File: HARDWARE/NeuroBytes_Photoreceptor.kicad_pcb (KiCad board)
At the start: 2 copper layers, 46.8 x 19.8 mm, 22 parts, among them P1 CONN_01X04, P2 CONN_01X04, P3 CONN_01X07, SW1 SW_PUSH, SW2 SW_PUSH, U1 APDS9007, U2 STM32L011Gx, U3 LD3985M33R

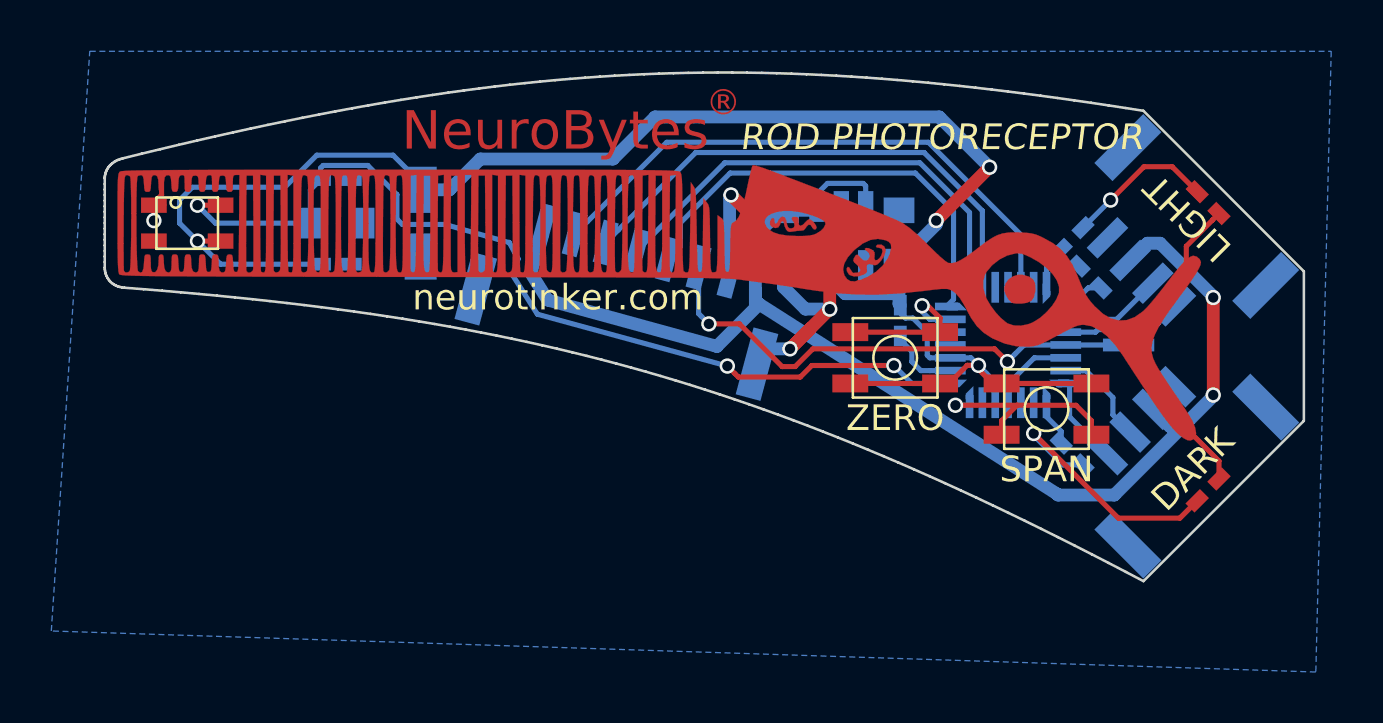
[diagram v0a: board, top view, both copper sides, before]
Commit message: Updated Gerber files. Added BOM. Added component values to schematic. Added fiducials.
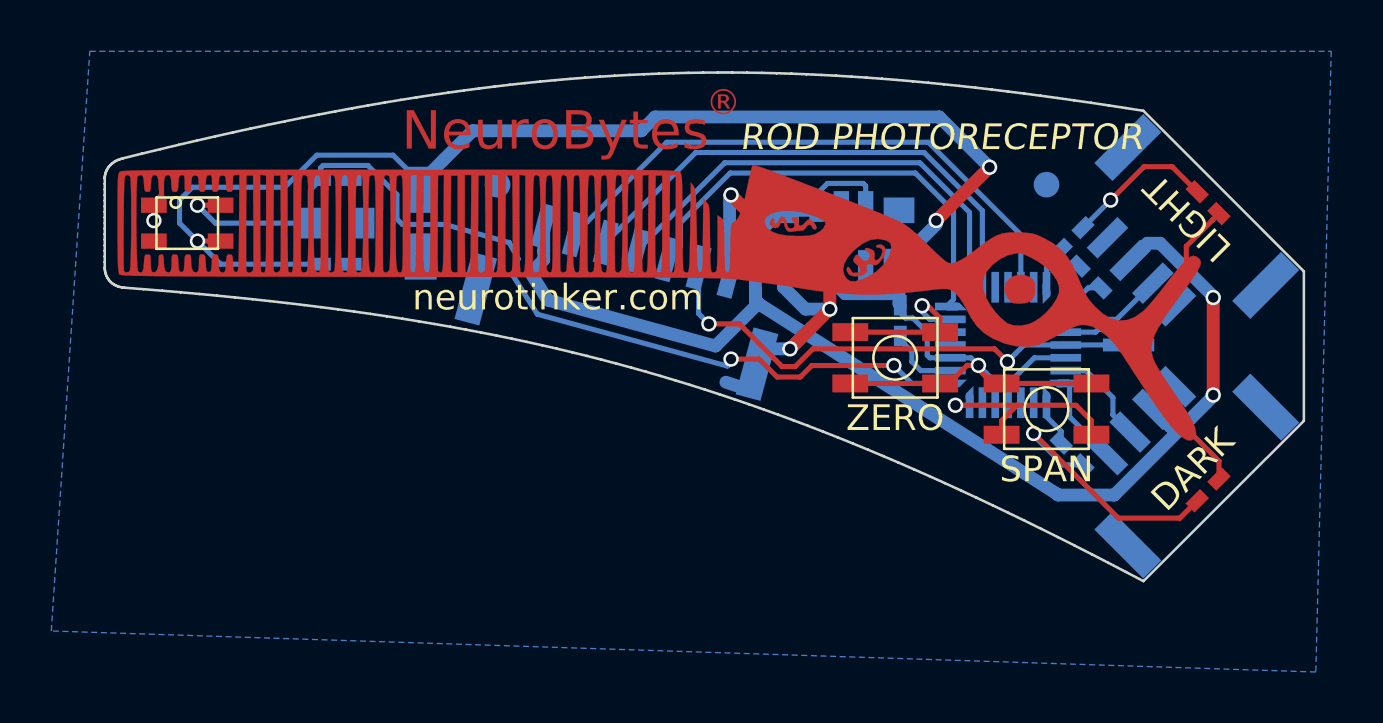
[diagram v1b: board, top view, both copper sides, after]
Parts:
- added REF**: ZF_Fiducial-1mm, KiCad_Footprints:ZF_Fiducial-1mm, B.Cu at (201.5, 94.5)
- added REF**: ZF_Fiducial-1mm, KiCad_Footprints:ZF_Fiducial-1mm, B.Cu at (180.1, 94.5)
- turned U1 to 270 degrees
- turned U2 to 270 degrees
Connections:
- P1 pad : (no net) -> GND
- P2 pad : (no net) -> GND
- P3 pad : (no net) -> GND
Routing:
- net GND: track 49.9 -> 51.9 mm
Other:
- board text added: "COMPONENT POSITION ORIGIN"
- board text added: "NOTES: 1. FOOTPRINTS ORIENTED PER IPC-7351FC LEVEL B (PIN 1 IN LOWER LEFT) 2. COMPONENT ROTATION IN DEGREES COUNTER-CLOCKWISE 3. NOTE COMPONENTS ARE MOUNTED ON BOTH F.CU AND B.CU LAYER 4. PCB IS 1.6mm FR4 RATED FOR ROHS REFLOW, 10Z COPPER, ENIG FINISH 5. MATTE BLACK SOLDER MASK WITH WHITE SILKSCREEN 6. SOLDER PASTE MUST BE ROHS COMPLIANT (LEAD-FREE) 7. NO MARKS (E-TEST, QA, SERIAL NUMBER, ETC) ON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"
- board text added: "ROUTE BOARD OUTLINE EXCEPT FOR TWO ENDS"
- board text added: "V-SCORE PARALLEL ENDS"

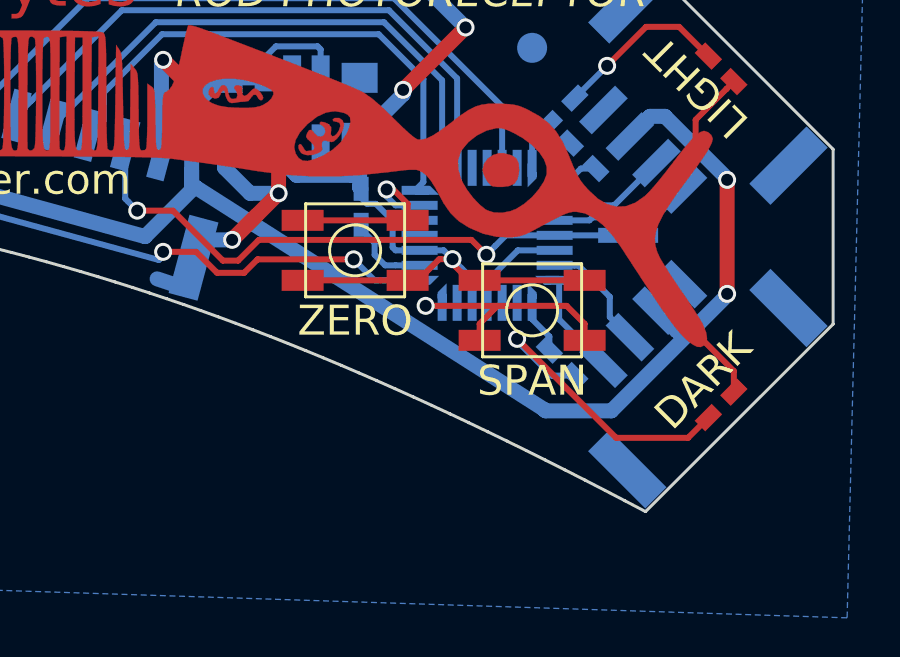
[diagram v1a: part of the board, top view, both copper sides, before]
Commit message: Updated swith footprint.
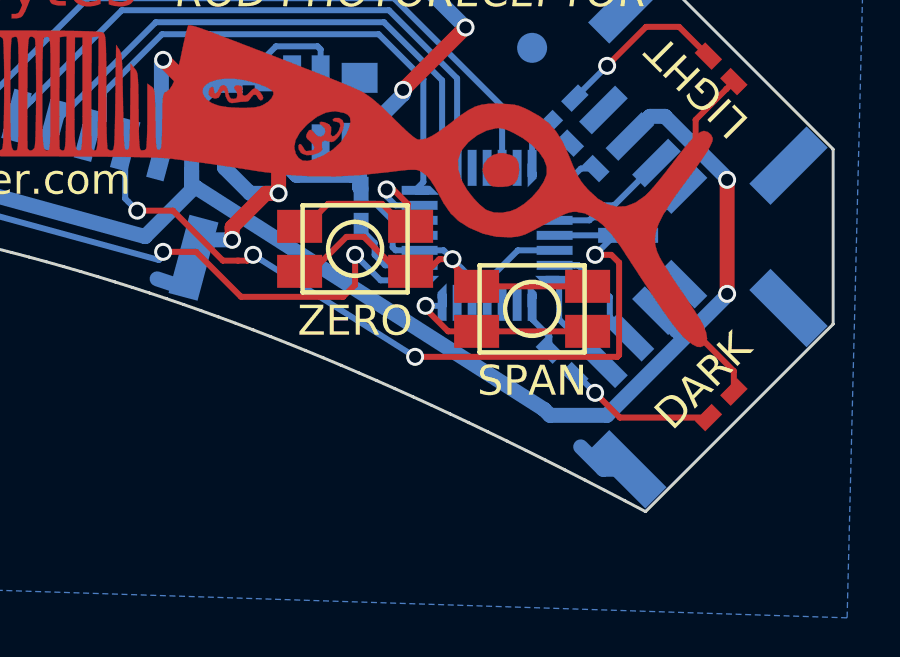
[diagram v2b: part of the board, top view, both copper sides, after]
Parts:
- C1, C2, C6: value C -> 100 nF
- C3, C4, C5: value C -> 1 uF
- C7: value CP -> 10 uF
- R1: value R -> 27k
- R2, R3: value R -> 10
- R4: value R -> JMP
- SW1, SW2: footprint KiCad_Footprints:ZF_SW_LS38 -> KiCad_Footprints:ZF_SW_EVP-AA
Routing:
- net RESET: track 20.0 -> 27.3 mm, vias 2 -> 4
- net Net-(D2-Pad2): track 10.5 -> 5.03 mm
- net SPAN: track 8.49 -> 7.00 mm
- net SENSE: track 37.9 -> 39.2 mm
- net +3V3: track 72.7 -> 74.1 mm
- net GND: track 51.9 -> 52.9 mm
- net ZERO: track 6.40 -> 7.22 mm

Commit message: Another switch footprint update
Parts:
- C1, C2, C6: value 100 nF -> 0u1
- C7: value 10 uF -> 10u; footprint KiCad_Footprints:ZF_SMD_pol_1206 -> KiCad_Footprints:ZF_SMD_nonpol_1206
- P1, P2: value CONN_01X04 -> JST_GH_4-POS
- P3: value CONN_01X07 -> JST_GH_7-POS
- R1: value 27k -> 10k
- SW1, SW2: value SW_PUSH -> SW_PB_4term; footprint KiCad_Footprints:ZF_SW_EVP-AA -> KiCad_Footprints:ZF_SW_PTS810
- moved P3 0.84 mm to (185.2, 98.6)
- moved P2 0.74 mm to (206.4, 104.8)
- moved P1 0.74 mm to (206.4, 96.8)
- moved SW2 0.61 mm to (201.6, 103.8), turned to 90 degrees
- moved SW1 0.41 mm to (195.2, 101.1), turned to 270 degrees
- moved C7 0.11 mm to (177.2, 96.0)
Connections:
- SW1 pad 1: +3V3 -> Net-(SW1-Pad1)
- SW2 pad 1: +3V3 -> Net-(SW2-Pad1)
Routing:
- net +3V3: track 74.1 -> 66.0 mm
- net ZERO: track 7.22 -> 2.77 mm
- net SPAN: track 7.00 -> 3.15 mm
- net GND: track 52.9 -> 55.9 mm
- net RESET: track 27.3 -> 25.3 mm
